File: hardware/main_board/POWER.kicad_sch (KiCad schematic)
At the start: 10 parts, among them IC201 LM2937ET-3.3_NOPB, J201 373

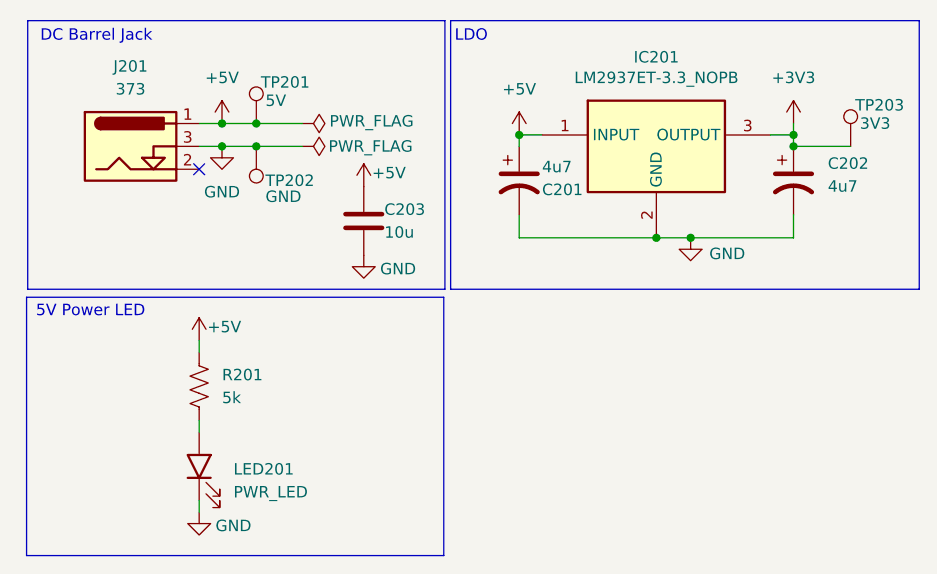
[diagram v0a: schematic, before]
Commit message: changed level shifter. bunch of aesthetic changes. led resistors changed on main board. saving before nuke mouser.co.uk
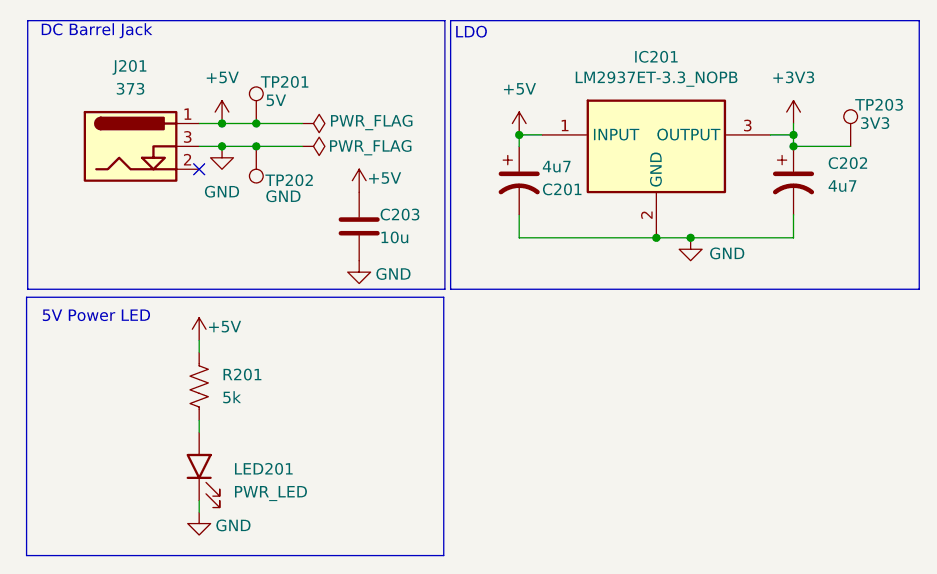
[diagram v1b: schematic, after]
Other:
- moved on the sheet: C203
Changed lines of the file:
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@@
 	(text "DC Barrel Jack"
 		(exclude_from_sim no)
-		(at 21.59 15.748 0)
+		(at 21.59 15.24 0)
 		(effects
 			(font
@@
 	(text "5V Power LED"
 		(exclude_from_sim no)
-		(at 20.955 46.355 0)
+		(at 21.59 46.99 0)
 		(effects
 			(font
@@
 	(text "LDO"
 		(exclude_from_sim no)
-		(at 63.246 15.748 0)
+		(at 63.246 15.494 0)
 		(effects
 			(font
@@
 	(symbol
 		(lib_id "power:+5V")
-		(at 51.3118 32.4207 0)
+		(at 50.8 33.02 0)
 		(unit 1)
 		(exclude_from_sim no)
@@
 		(dnp no)
 		(property "Reference" "#PWR0202"
-			(at 51.3118 36.2307 0)
+			(at 50.8 36.83 0)
 			(effects
 				(font
@@
 		)
 		(property "Value" "+5V"
-			(at 54.1058 30.8967 0)
+			(at 53.594 31.496 0)
 			(effects
 				(font
@@
 		)
 		(property "Footprint" ""
-			(at 51.3118 32.4207 0)
+			(at 50.8 33.02 0)
 			(effects
 				(font
@@
 		)
 		(property "Datasheet" ""
-			(at 51.3118 32.4207 0)
+			(at 50.8 33.02 0)
 			(effects
 				(font
@@
 		)
 		(property "Description" "Power symbol creates a global label with name \"+5V\""
-			(at 51.3118 32.4207 0)
+			(at 50.8 33.02 0)
 			(effects
 				(font
@@
 	(symbol
 		(lib_id "power:GND")
-		(at 51.3118 40.0407 0)
+		(at 50.8 40.64 0)
 		(unit 1)
 		(exclude_from_sim no)
@@
 		(dnp no)
 		(property "Reference" "#PWR0201"
-			(at 51.3118 46.3907 0)
+			(at 50.8 46.99 0)
 			(effects
 				(font
@@
 		)
 		(property "Value" "GND"
-			(at 55.1218 41.5647 0)
+			(at 54.61 42.164 0)
 			(effects
 				(font
@@
 		)
 		(property "Footprint" ""
-			(at 51.3118 40.0407 0)
+			(at 50.8 40.64 0)
 			(effects
 				(font
@@
 		)
 		(property "Datasheet" ""
-			(at 51.3118 40.0407 0)
+			(at 50.8 40.64 0)
 			(effects
 				(font
@@
 		)
 		(property "Description" "Power symbol creates a global label with name \"GND\" , ground"
-			(at 51.3118 40.0407 0)
+			(at 50.8 40.64 0)
 			(effects
 				(font
@@
 	(symbol
 		(lib_id "ECE445L:C")
-		(at 51.3118 36.2307 0)
+		(at 50.8 36.83 0)
 		(unit 1)
 		(exclude_from_sim no)
@@
 		(dnp no)
 		(property "Reference" "C203"
-			(at 53.5978 34.9607 0)
+			(at 53.086 35.56 0)
 			(effects
 				(font
@@
 		)
 		(property "Value" "10u"
-			(at 53.5978 37.5007 0)
+			(at 53.086 38.1 0)
 			(effects
 				(font
@@
 		)
 		(property "Footprint" "Capacitor_SMD:C_0805_2012Metric"
-			(at 52.277 40.0407 0)
+			(at 51.7652 40.64 0)
 			(effects
 				(font
@@
 		)
 		(property "Datasheet" "~"
-			(at 51.3118 36.2307 0)
+			(at 50.8 36.83 0)
 			(effects
 				(font
@@
 		)
 		(property "Description" "Unpolarized capacitor"
-			(at 51.3118 36.2307 0)
-			(effects
-				(font
+			(at 50.8 36.83 0)
+			(effects
+				(font

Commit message: finished everything except bom information. drc verification
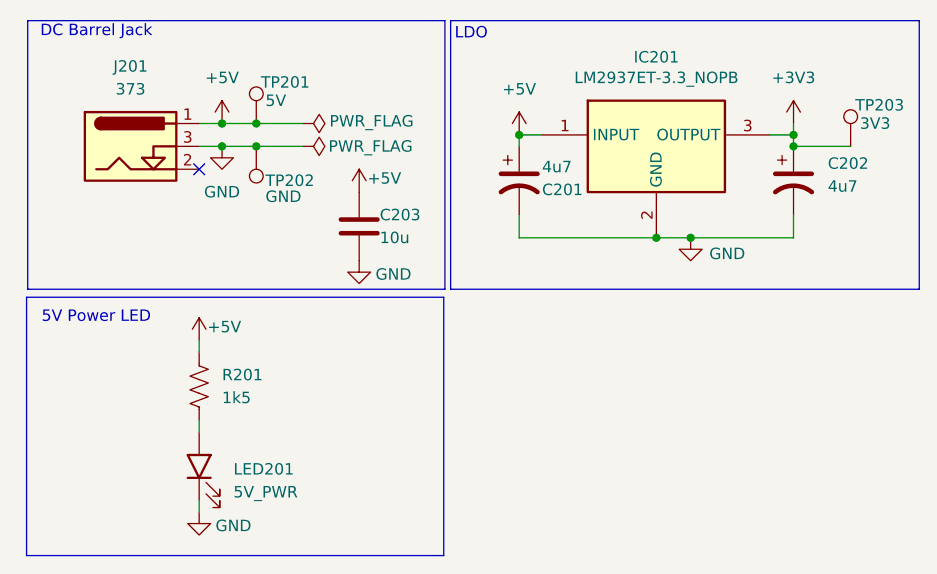
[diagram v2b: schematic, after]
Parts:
- IC201: Mouser Price/Stock https://www.mouser.co.uk/ProductDetail/Texas-Instruments/LM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 -> https://www.mouser.com/ProductDetail/Texas-Instruments/LM29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
- J201: Mouser Price/Stock https://www.mouser.co.uk/ProductDetail/Adafruit/373?qs=GURa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 -> https://www.mouser.com/ProductDetail/Adafruit/373?qs=GURawf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
- LED201: value PWR_LED -> 5V_PWR; Mouser Price/Stock https://www.mouser.co.uk/ProductDetail/ams-OSRAM/LS-R976-NR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 -> https://www.mouser.com/ProductDetail/ams-OSRAM/LS-R976-NR-1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
- R201: value 5k -> 1k5
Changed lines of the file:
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@@
 			)
 		)
-		(property "Mouser Price/Stock" "https://www.mouser.co.uk/ProductDetail/Adafruit/373?qs=GURawfaeGuDDC%2FyE6Usrdw%3D%3D"
+		(property "Mouser Price/Stock" "https://www.mouser.com/ProductDetail/Adafruit/373?qs=GURawfaeGuDDC%2FyE6Usrdw%3D%3D"
 			(at 41.91 620.32 0)
 			(effects
@@
 			)
 		)
-		(property "Mouser Price/Stock" "https://www.mouser.co.uk/ProductDetail/Texas-Instruments/LM2937ET-3.3-NOPB?qs=X1J7HmVL2ZEMUke2IfNR4w%3D%3D"
+		(property "Mouser Price/Stock" "https://www.mouser.com/ProductDetail/Texas-Instruments/LM2937ET-3.3-NOPB?qs=X1J7HmVL2ZEMUke2IfNR4w%3D%3D"
 			(at 92.71 620.32 0)
 			(effects
@@
 			)
 		)
-		(property "Value" "5k"
+		(property "Value" "1k5"
 			(at 35.56 55.8799 0)
 			(effects
@@
 			)
 		)
-		(property "Value" "PWR_LED"
+		(property "Value" "5V_PWR"
 			(at 36.83 66.3574 0)
 			(effects
@@
 			)
 		)
-		(property "Mouser Price/Stock" "https://www.mouser.co.uk/ProductDetail/ams-OSRAM/LS-R976-NR-1?qs=K5ta8V%252BWhtZhvCAe1sTZFg%3D%3D"
+		(property "Mouser Price/Stock" "https://www.mouser.com/ProductDetail/ams-OSRAM/LS-R976-NR-1?qs=K5ta8V%252BWhtZhvCAe1sTZFg%3D%3D"
 			(at 46.99 657.15 0)
 			(effects

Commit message: led info
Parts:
- C201: Mouser Price/Stock https://www.mouser.com/ProductDetail/KYOCERA-AVX/0805YC105K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 -> (none)
- C202: Mouser Price/Stock https://www.mouser.com/ProductDetail/KYOCERA-AVX/TCP1A106M8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 -> (none)
- C203: Mouser Price/Stock (none) -> https://www.mouser.com/ProductDetail/Samsung-Electro-Mechan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
- LED201: Mouser Price/Stock https://www.mouser.com/ProductDetail/ams-OSRAM/LS-R976-NR-1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 -> https://www.mouser.com/ProductDetail/LITEON/LTST-C170EKT?qs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
- R201: Mouser Price/Stock (none) -> https://www.mouser.com/ProductDetail/ROHM-Semiconductor/ESR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
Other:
- note added: "RED"
- moved on the sheet: LED201
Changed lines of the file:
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@@
+		)
+	)
+	(text "RED"
+		(exclude_from_sim no)
+		(at 38.1 65.278 0)
+		(effects
+			(font
+				(size 1.27 1.27)
+			)
 		)
 	)
@@
 	(wire
 		(pts
-			(xy 33.02 68.58) (xy 33.02 67.31)
+			(xy 33.02 68.58) (xy 33.02 66.04)
 		)
 		(stroke
@@
 		(pts
 			(xy 68.58 26.67) (xy 71.12 26.67)
-		)
-		(stroke
-			(width 0)
-			(type default)
-		)
-	)
-	(wire
-		(pts
-			(xy 33.02 58.42) (xy 33.02 59.69)
 		)
 		(stroke
@@
 			)
 		)
+		(property "Mouser Price/Stock" "https://www.mouser.com/ProductDetail/ROHM-Semiconductor/ESR03EZPJ152?qs=DyUWGjl%252BcVvm2NOHIcQYzQ%3D%3D"
+			(at 33.02 54.61 0)
+			(effects
+				(font
+					(size 1.27 1.27)
+				)
+				(hide yes)
+			)
+		)
 		(pin "1"
 		)
@@
 			)
 		)
-		(property "Mouser Price/Stock" "https://www.mouser.com/ProductDetail/KYOCERA-AVX/TCP1A106M8R?qs=sGAEpiMZZMtZ1n0r9vR22blfza6EDqdqKChrjBJniGMwR4ZbZ0PzAQ%3D%3D"
+		(property "Mouser Price/Stock" ""
 			(at 99.06 31.75 0)
 			(effects
@@
 	(symbol
 		(lib_id "ECE445L:LED")
-		(at 34.29 63.5 0)
+		(at 34.29 62.23 0)
 		(unit 1)
 		(exclude_from_sim no)
@@
 		(on_board yes)
 		(dnp no)
-		(fields_autoplaced yes)
 		(property "Reference" "LED201"
-			(at 36.83 63.8174 0)
+			(at 36.068 60.452 0)
 			(effects
 				(font
@@
 		)
 		(property "Value" "5V_PWR"
-			(at 36.83 66.3574 0)
+			(at 36.068 62.992 0)
 			(effects
 				(font
@@
 		)
 		(property "Footprint" "SamacSys_Parts:LEDC2012X40N"
-			(at 46.99 157.15 0)
+			(at 46.99 155.88 0)
 			(effects
 				(font
@@
 			)
 		)
-		(property "Datasheet" "https://datasheet.datasheetarchive.com/originals/distributors/DKDS-18/344792.pdf"
-			(at 46.99 257.15 0)
+		(property "Datasheet" ""
+			(at 46.99 255.88 0)
 			(effects
 				(font
@@
 		)
 		(property "Description" "Standard LEDs - SMD Super Red, 633nm 180mcd, 20mA"
-			(at 34.29 63.5 0)
+			(at 34.29 62.23 0)
 			(effects
 				(font
@@
 		)
 		(property "Height" "0.4"
-			(at 46.99 457.15 0)
+			(at 46.99 455.88 0)
 			(effects
 				(font
@@
 		)
 		(property "Mouser Part Number" "720-LSR976-NR-1"
-			(at 46.99 557.15 0)
+			(at 46.99 555.88 0)
 			(effects
 				(font
@@
 			)
 		)
-		(property "Mouser Price/Stock" "https://www.mouser.com/ProductDetail/ams-OSRAM/LS-R976-NR-1?qs=K5ta8V%252BWhtZhvCAe1sTZFg%3D%3D"
-			(at 46.99 657.15 0)
+		(property "Mouser Price/Stock" "https://www.mouser.com/ProductDetail/LITEON/LTST-C170EKT?qs=sGAEpiMZZMv0DJfhVcWlKzTPaP0s1oGosckfGozvZMw%3D"
+			(at 46.99 655.88 0)
 			(effects
 				(font
@@
 		)
 		(property "Manufacturer_Name" "ams OSRAM"
-			(at 46.99 757.15 0)
+			(at 46.99 755.88 0)
 			(effects
 				(font
@@
 		)
 		(property "Manufacturer_Part_Number" "LS R976-NR-1"
-			(at 46.99 857.15 0)
+			(at 46.99 855.88 0)
 			(effects
 				(font
@@
 			)
 		)
+		(property "Mouser Price/Stock" "https://www.mouser.com/ProductDetail/Samsung-Electro-Mechanics/CL21A106KPFNNNE?qs=sGAEpiMZZMt7gvpyg0xT8jBAVP%252BdkPhuUJvUBe19zr8%3D"
+			(at 50.8 36.83 0)
+			(effects
+				(font
+					(size 1.27 1.27)
+				)
+				(hide yes)
+			)
+		)
 		(pin "1"
 		)
@@
 			)
 		)
-		(property "Datasheet" "https://datasheets.kyocera-avx.com/KGM_X7R.pdf"
+		(property "Datasheet" "~"
 			(at 68.58 31.75 0)
 			(effects
@@
 			)
 		)
-		(property "Mouser Price/Stock" "https://www.mouser.com/ProductDetail/KYOCERA-AVX/0805YC105KAT2A?qs=Ppq%252BQS%252B9qgKbltvIecMi5g%3D%3D"
+		(property "Mouser Price/Stock" ""
 			(at 68.58 31.75 0)
 			(effects
